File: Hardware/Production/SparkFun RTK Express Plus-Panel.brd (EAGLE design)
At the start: 219.3 x 141.9 mm, 510 parts, among them J13 Internal, J16 MICRO-SD-PUSH-PUSH-EXT-PIN, J17 Qwiic Right Angle, J19 External, J21 USB Female Type C Connector, J24 USB Female Type C Connector, J3 USB Female Type C Connector, J31 Qwiic Right Angle, J32 Internal, J38 MICRO-SD-PUSH-PUSH-EXT-PIN, J39 External, J4 External, J40 USB Female Type C Connector, J43 USB Female Type C Connector, J5 USB Female Type C Connector, J50 Qwiic Right Angle, J51 Internal, J57 MICRO-SD-PUSH-PUSH-EXT-PIN, Q1 SIL2308-TP, Q2 MBT3904DW1T1, Q3 MBT3904DW1T1, Q4 SIL2308-TP, Q5 MBT3904DW1T1, Q6 SIL2308-TP, U1 74HC4052D, U10 MCP73833, U11 U-BLOX_ZED_F9R, U12 CH340C, U13 LIS2DH12, U14 MAX17048, U15 STLQ015-3.3V, U16 MCP73833, U17 74HC4052D, U18 LIS2DH12, U19 ESP-WROOM-3232D-NARROW, U2 AP2112K-3.3, U20 NC7SZ14-D, U21 NC7SZ14-D, U22 U-BLOX_ZED_F9R, U23 AP2112K-3.3, U24 CH340C, U25 MAX17048, U26 STLQ015-3.3V, U27 MCP73833, U28 74HC4052D, U29 LIS2DH12, U3 AP2112K-3.3, U30 ESP-WROOM-3232D-NARROW, U31 NC7SZ14-D, U32 NC7SZ14-D, U33 U-BLOX_ZED_F9R, U4 STLQ015-3.3V, U5 ESP-WROOM-3232D-NARROW, U6 CH340C, U7 MAX17048, U8 NC7SZ14-D, U9 NC7SZ14-D

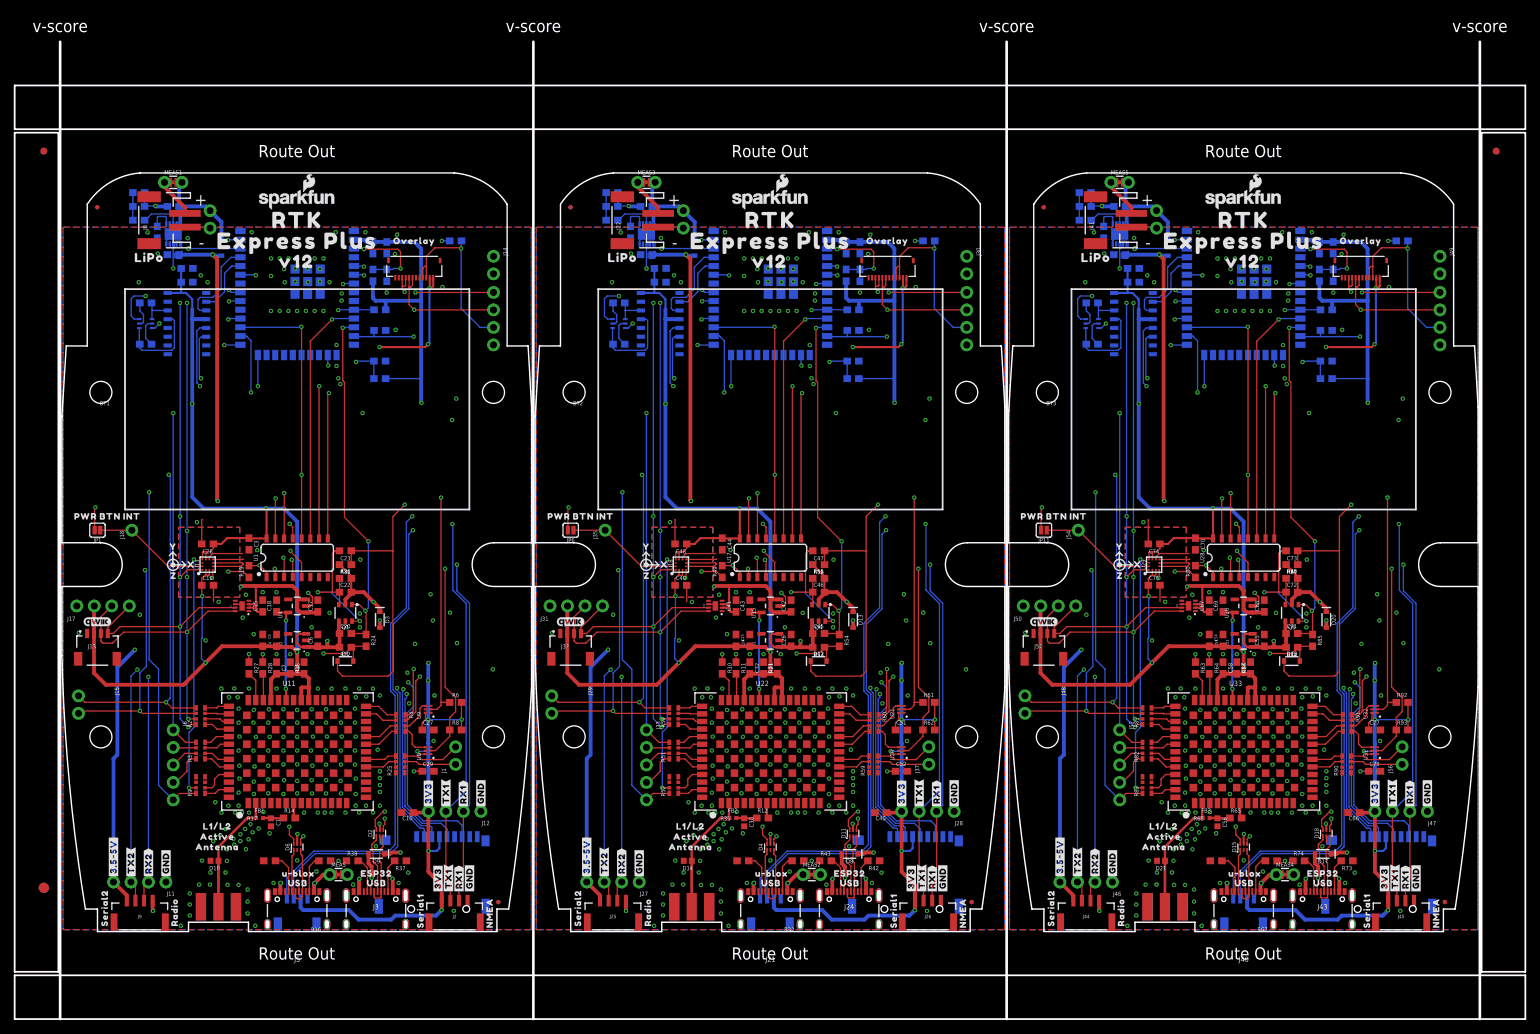
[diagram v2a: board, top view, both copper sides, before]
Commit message: v13 - Change to LIF overlay connector. Change ESP32 FP. Pull ground from accel.
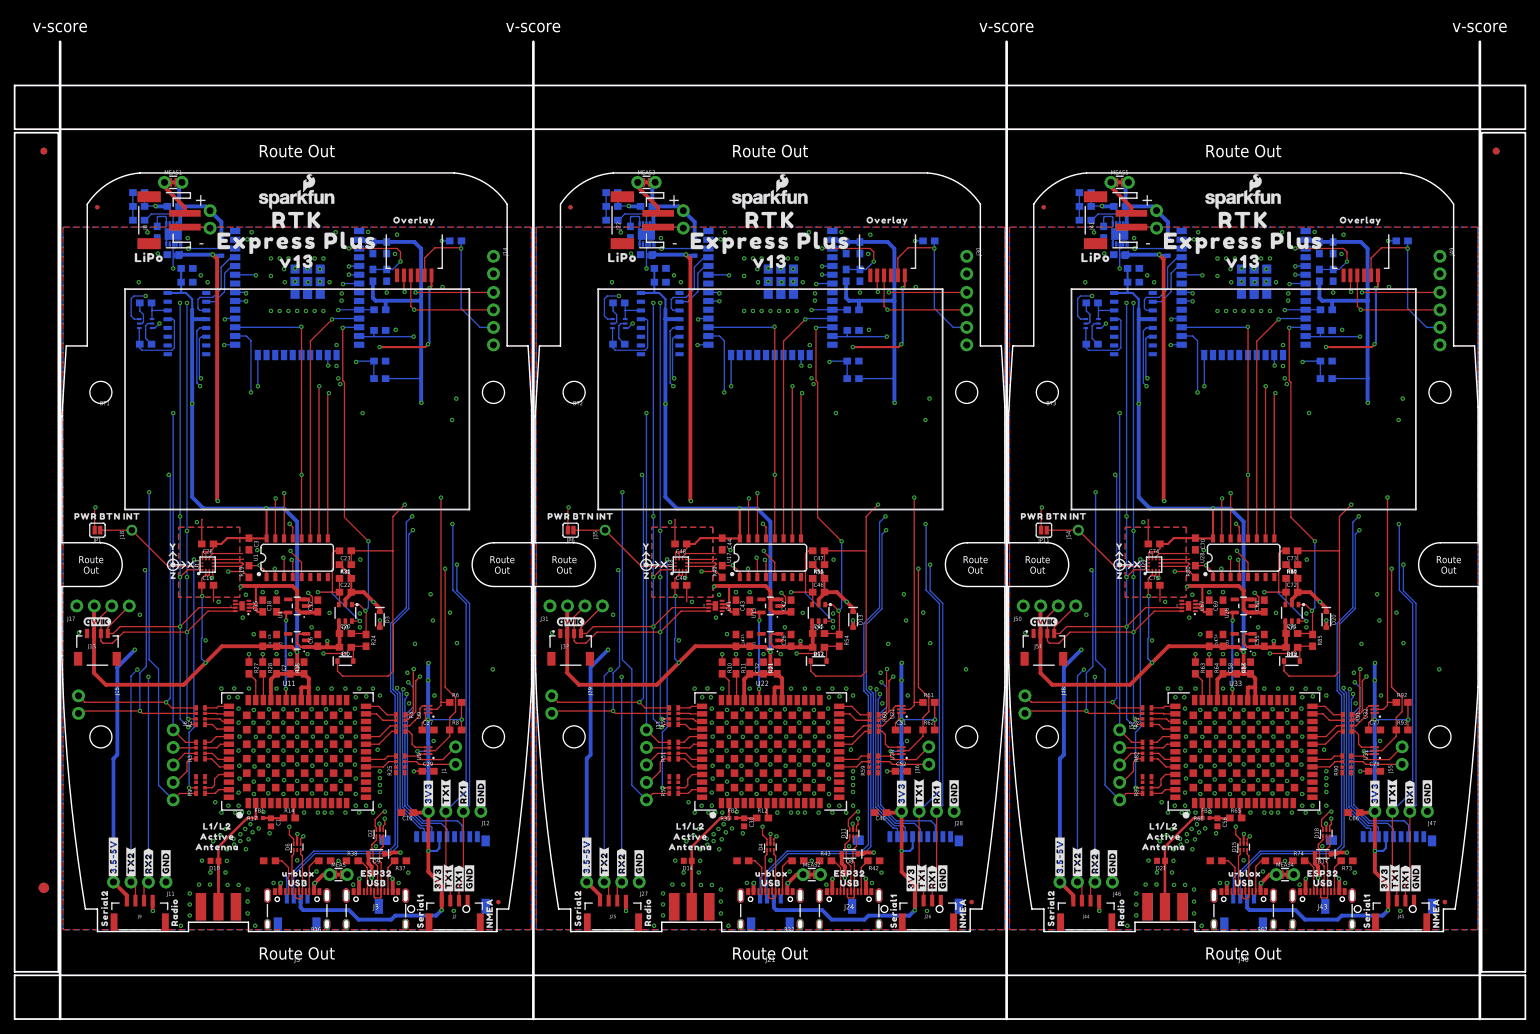
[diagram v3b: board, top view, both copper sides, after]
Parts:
- D10, D14, D21: value PESD0402 -> PESD0402-0402
- J19: value External -> (none); device SparkFun-Connectors:JST04_1MM_RA -> SparkFun-Connectors:FPC_6_1MM-LIF
- J20: value (none) -> External; device RTK Facet:FPC_12_DOUBLESIDED_BACKFLIP -> SparkFun-Connectors:JST04_1MM_RA
- J36, J55: device RTK Facet:FPC_12_DOUBLESIDED_BACKFLIP -> SparkFun-Connectors:1X02_NO_SILK
- J37, J56: value (none) -> MICRO-SD-PUSH-PUSH-EXT-PIN; device SparkFun-Connectors:1X02_NO_SILK -> SparkFun-Connectors:MICROSD-EXTERNALPIN
- J38, J57: value MICRO-SD-PUSH-PUSH-EXT-PIN -> (none); device SparkFun-Connectors:MICROSD-EXTERNALPIN -> SparkFun-Connectors:FPC_6_1MM-LIF
- JP1, JP11, JP6: value (none) -> JUMPER-SMT_2_NO_SILK
- MEAS, MEAS1, MEAS2, MEAS3, MEAS4, MEAS5: value (none) -> JUMPER-COMBO_2_NC_TRACE
- U$1: device SparkFun-Aesthetics:QWIIC_4MM -> output:V130
- U$118, U$177: device output:V120 -> output:V130
- U$18: device SparkFun GPS RTK Surveyor:1553DBK-ENCLOSURE -> output:#RTK#1
- U$19: device output:V120 -> SparkFun GPS RTK Surveyor:1553DBK-ENCLOSURE
- U$2: device output:#RTK#1 -> SparkFun-Aesthetics:QWIIC_4MM
- U19, U30, U5: value ESP-WROOM-3232D-NARROW -> ESP-WROOM-3232D; device SparkFun-RF:ESP-WROOM-32D-NARROW -> SparkFun-RF:ESP-WROOM-32D
- moved U$1 113.7 mm to (34.2, 97.3), flipped to the top
- moved J19 106.9 mm to (51.2, 98.3), flipped to the top, turned to 180 degrees
- moved J20 105.1 mm to (102.9, 4.74), flipped to the bottom, turned to 0 degrees
- moved J38 95.0 mm to (119.9, 98.3), flipped to the top, turned to 180 degrees
- moved J57 95.0 mm to (188.6, 98.3), flipped to the top, turned to 180 degrees
- moved U$19 81.7 mm to (102.9, 53.3), turned to 90 degrees
- moved J36 72.2 mm to (125.9, 24.3), turned to 90 degrees
- moved J55 72.2 mm to (194.6, 24.3), turned to 90 degrees
- moved U$18 34.8 mm to (125.4, 26.8), flipped to the bottom, turned to 0 degrees
- moved U$2 30.2 mm to (102.9, 6.65)
- moved J37 21.3 mm to (122.5, 3.27), flipped to the bottom, turned to 0 degrees
- moved J56 21.3 mm to (191.2, 3.27), flipped to the bottom, turned to 0 degrees
- moved U$112 3.00 mm to (119.9, 103.3)
- moved U$171 3.00 mm to (188.6, 103.3)
- moved U$8 3.00 mm to (51.2, 103.3)
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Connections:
- net ESP_19/CIPO renamed ESP_19/POCI
- net ESP_23/COPI renamed ESP_23/PICO
- removed net ESP_19/CIPO1: J38.7, U19.31
- removed net ESP_19/CIPO2: J57.7, U30.31
- removed net ESP_23/COPI1: J38.3, U19.37
- removed net ESP_23/COPI2: J57.3, U30.37
- new net ESP_19/POCI1: J37.7, U19.31
- new net ESP_19/POCI2: J56.7, U30.31
- new net ESP_23/PICO1: J37.3, U19.37
- new net ESP_23/PICO2: J56.3, U30.37
- net 3.3V1: now also J20.2, J37.4; no longer J19.2, J38.4
- net 3.3V2: now also J56.4; no longer J57.4
- net CHG_LED_RES: now also J19.2; no longer J20.3, J20.4
- net CHG_LED_RES1: now also J38.2; no longer J36.3, J36.4
- net CHG_LED_RES2: now also J57.2; no longer J55.3, J55.4
- net ESP_14/SETUP_BUTTON: now also J19.4; no longer J20.7, J20.8
- net ESP_14/SETUP_BUTTON1: now also J38.4; no longer J36.7, J36.8
- net ESP_14/SETUP_BUTTON2: now also J57.4; no longer J55.7, J55.8
- net ESP_18/SCK1: now also J37.5; no longer J38.5
- net ESP_18/SCK2: now also J56.5; no longer J57.5
- net ESP_21/SDA1: now also J20.3; no longer J19.3
- net ESP_22/SCL1: now also J20.4; no longer J19.4
- net ESP_25/SD_!CS!1: now also J37.2; no longer J38.2
- net ESP_25/SD_!CS!2: now also J56.2; no longer J57.2
- net GND: now also J19.6, U5.GND; no longer J20.11, J20.12, U5.GND1
- net GND1: now also J20.1, J37.10, J37.11, J37.12, J37.13, J37.6, U19.GND; no longer J19.1, J36.11, J36.12, J38.10, J38.11, J38.12, J38.13, U19.GND1
- net GND2: now also J56.10, J56.11, J56.12, J56.13, J56.6, U30.GND; no longer J55.11, J55.12, J57.10, J57.11, J57.12, J57.13, U30.GND1
- net POWER_BTN: now also J19.5; no longer J20.10, J20.9
- net POWER_BTN1: now also J38.5; no longer J36.10, J36.9
- net POWER_BTN2: now also J57.5; no longer J55.10, J55.9
- net V_USB: now also J19.1; no longer J20.1, J20.2
- net V_USB1: now also J38.1; no longer J36.1, J36.2
- net V_USB2: now also J57.1; no longer J55.1, J55.2
- net ZED_FENCE_STAT1: now also J36.1; no longer J37.1
- net ZED_FENCE_STAT2: now also J55.1; no longer J56.1
- net ZED_RTK_STAT1: now also J36.2; no longer J37.2
- net ZED_RTK_STAT2: now also J55.2; no longer J56.2
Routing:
- net ESP_23/COPI1: track 112.7 -> 0.00 mm, vias 3 -> 0
- net ESP_23/COPI2: track 112.7 -> 0.00 mm, vias 3 -> 0
- net ESP_19/CIPO2: track 110.1 -> 0.00 mm, vias 3 -> 0
- net ESP_19/CIPO1: track 110.1 -> 0.00 mm, vias 3 -> 0
- net ESP_23/PICO1: track 0.00 -> 109.9 mm, vias 0 -> 3
- net ESP_23/PICO2: track 0.00 -> 109.9 mm, vias 0 -> 3
- net ESP_19/POCI2: track 0.00 -> 107.2 mm, vias 0 -> 3
- net ESP_19/POCI1: track 0.00 -> 107.2 mm, vias 0 -> 3
- net ESP_19/POCI: track 110.1 -> 107.2 mm
- net ESP_23/PICO: track 112.7 -> 109.9 mm
- net ESP_18/SCK: track 106.7 -> 104.1 mm
- net ESP_18/SCK1: track 106.7 -> 104.1 mm
- net ESP_18/SCK2: track 106.7 -> 104.1 mm
- net CHG_LED_RES2: track 26.4 -> 24.1 mm
- net CHG_LED_RES1: track 26.4 -> 24.1 mm
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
